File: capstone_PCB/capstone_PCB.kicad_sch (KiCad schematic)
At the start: 43 parts, among them J1 282837-4, J2 282837-4, J3 Barrel Jack, J4 282837-4, J5 Fan1, J6 Fan2, J7 12402012E212A, P1 282837-2, P3 282837-2, P4 282837-2, P5 282837-2, Q1 IRF4905PBF, U1 DEV-15583, U2 2472, U3 VNH5019ATR-E, U4 VNH5019ATR-E

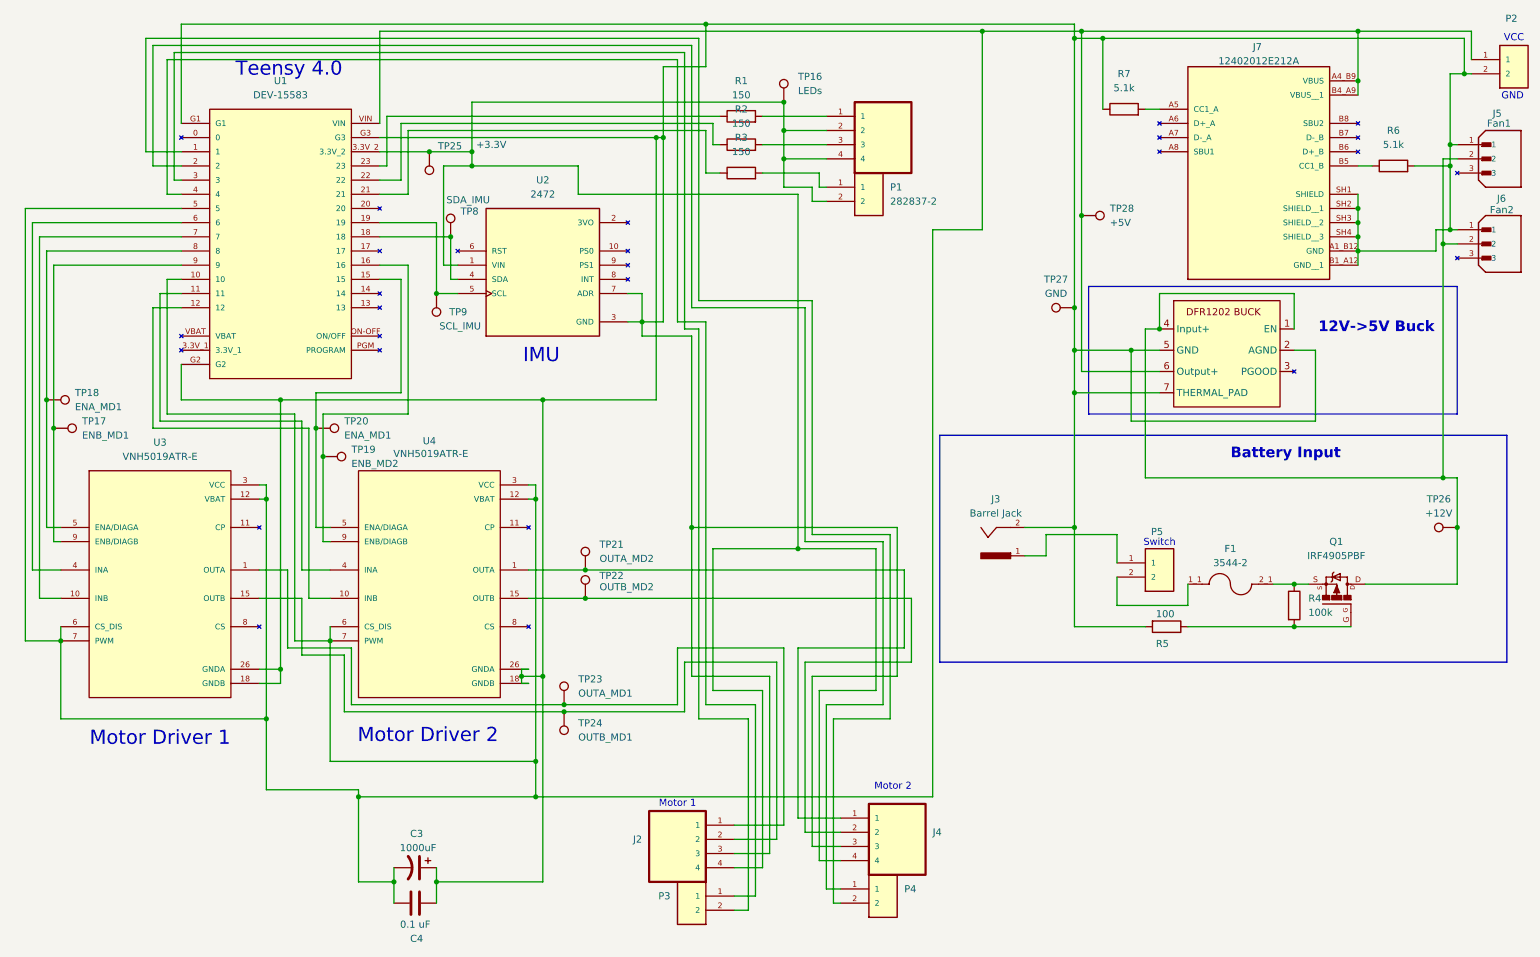
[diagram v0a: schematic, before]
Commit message: Updated Capstone PCB to new iteration with esp32
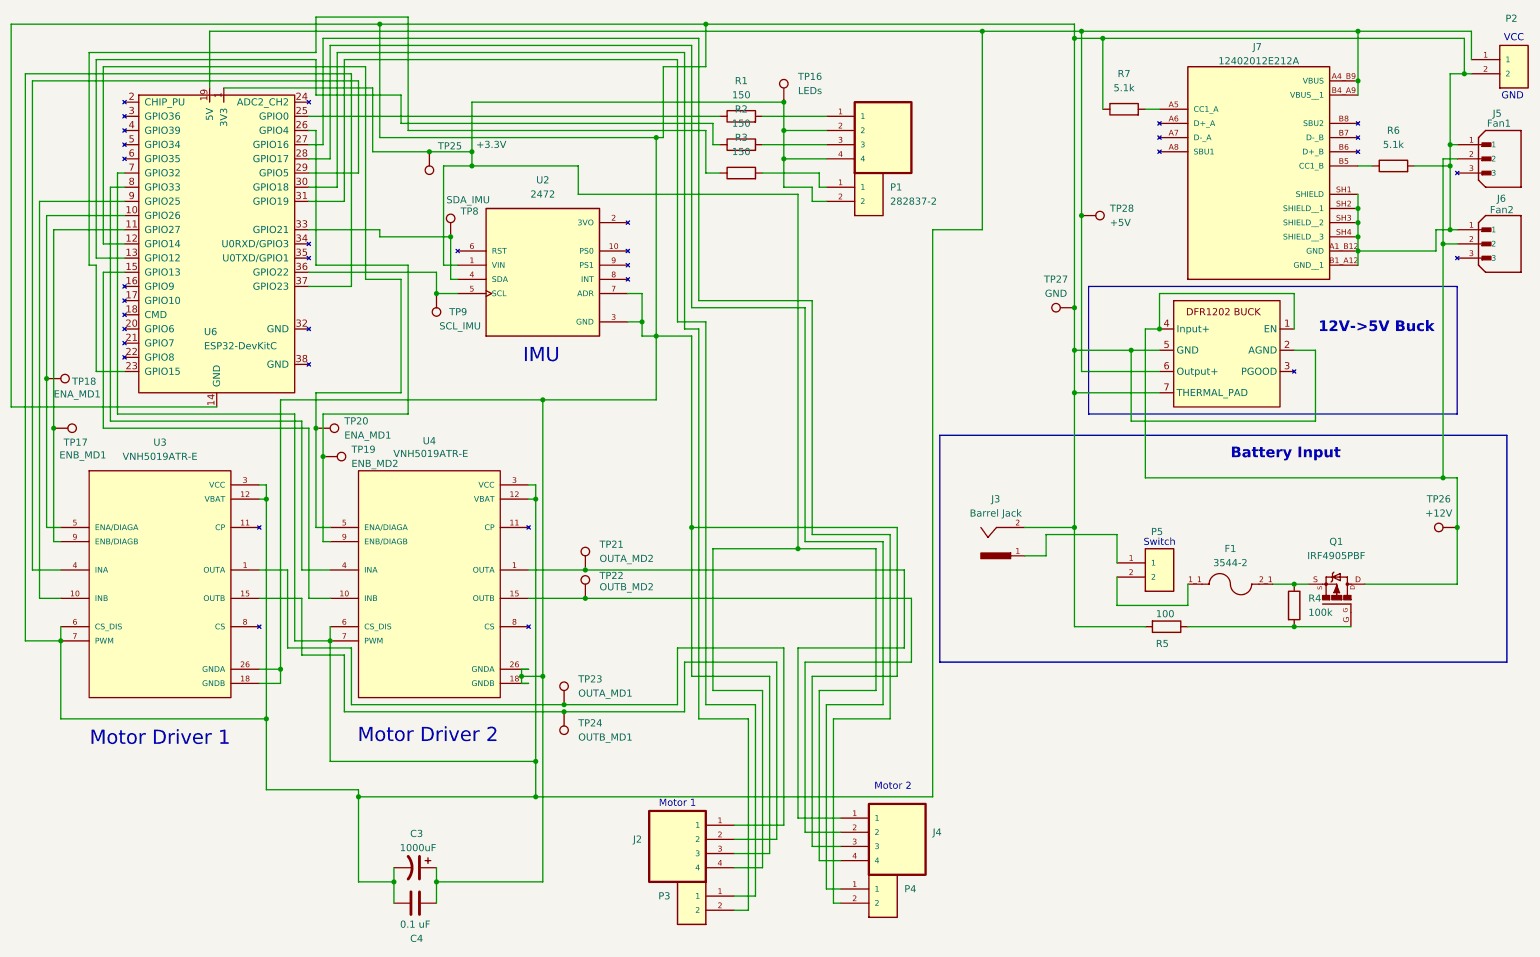
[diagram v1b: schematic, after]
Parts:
- removed U1: DEV-15583, DEV-15583:MODULE_DEV-15583, symbol DEV-15583:DEV-15583
- added U6: ESP32-DevKitC, PCM_Espressif:ESP32-DevKitC, symbol PCM_Espressif:ESP32-DevKitC
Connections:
- net GNDA: now also U6.14 (GND)
- net VCC: now also U6.19 (5V), U6.37 (GPIO23), U6.7 (GPIO32)
- net at P3.1: now also U6.31 (GPIO19)
- net at P3.2: now also U6.30 (GPIO18)
- net at P4.2: now also U6.27 (GPIO16)
- net at U4.4 (INA): now also U6.8 (GPIO33)
- net at U4.10 (INB): now also U6.15 (GPIO13)
- net at TP20.1, U4.5 (ENA/DIAGA): now also U6.12 (GPIO14)
- net at TP19.1, U4.9 (ENB/DIAGB): now also U6.26 (GPIO4)
- net at TP8.1, U2.4 (SDA): now also U6.33 (GPIO21)
- net at TP9.1, U2.5 (SCL): now also U6.36 (GPIO22)
- net at P4.1: now also U6.28 (GPIO17)
- net at R3.1: now also U6.23 (GPIO15)
- net at R2.1: now also U6.13 (GPIO12)
- net at R1.1: now also U6.25 (GPIO0)
- net at J1.2, J1.4, J2.4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: now also U6.1 (3V3)
- net at U3.4 (INA): now also U6.29 (GPIO5)
- net at U3.10 (INB): now also U6.9 (GPIO25)
- net at TP18.1, U3.5 (ENA/DIAGA): now also U6.10 (GPIO26)
- net at TP17.1, U3.9 (ENB/DIAGB): now also U6.11 (GPIO27)
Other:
- note removed: "Teensy 4.0"
- moved on the sheet: TP18
